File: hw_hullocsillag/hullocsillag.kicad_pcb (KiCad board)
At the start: 2 copper layers, 110 x 56 mm, 38 parts, among them J1 Conn_2Rows-05Pins, Q1 AO3401A, Q2 AO3401A, Q3 AO3401A, SW2 SW_DPST_x2, T1 Tab, T2 Tab, T3 Tab, U1 PY32F002AF15P6TU

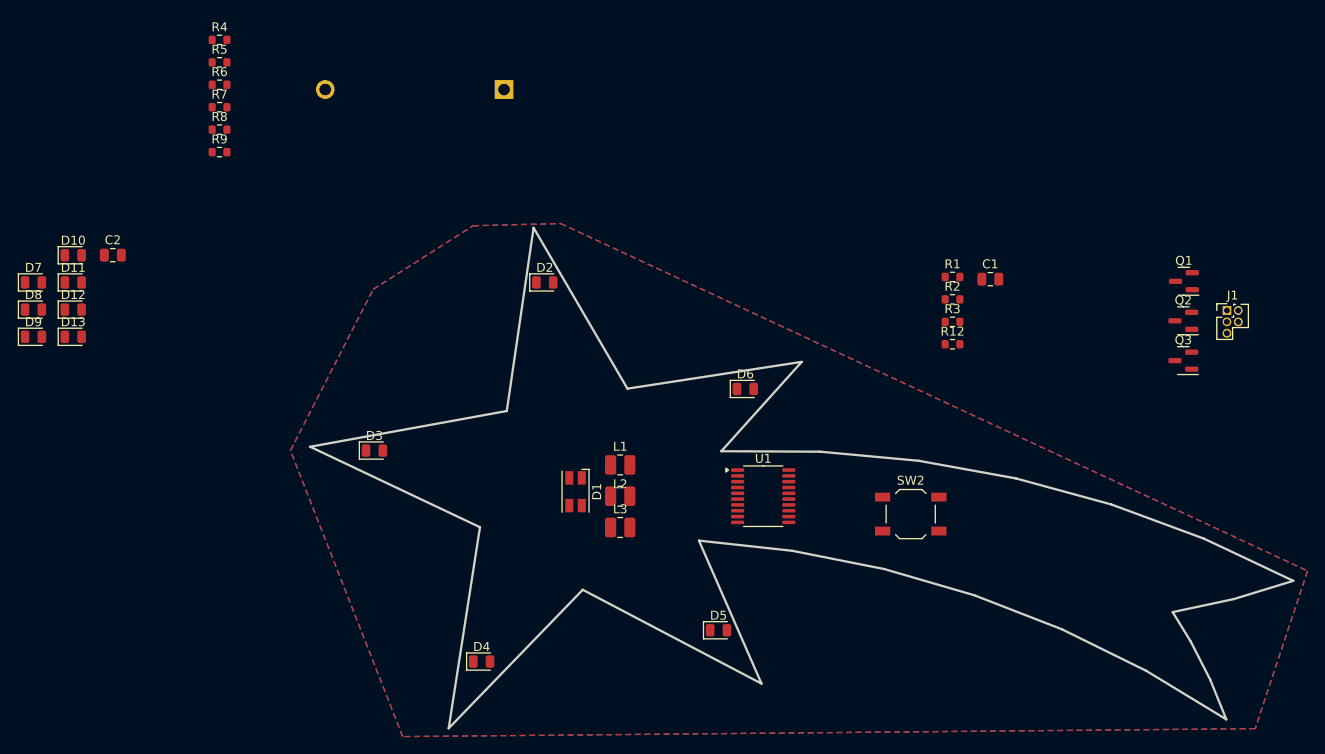
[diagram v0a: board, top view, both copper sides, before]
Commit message: Hullocsillag updated, new led driver
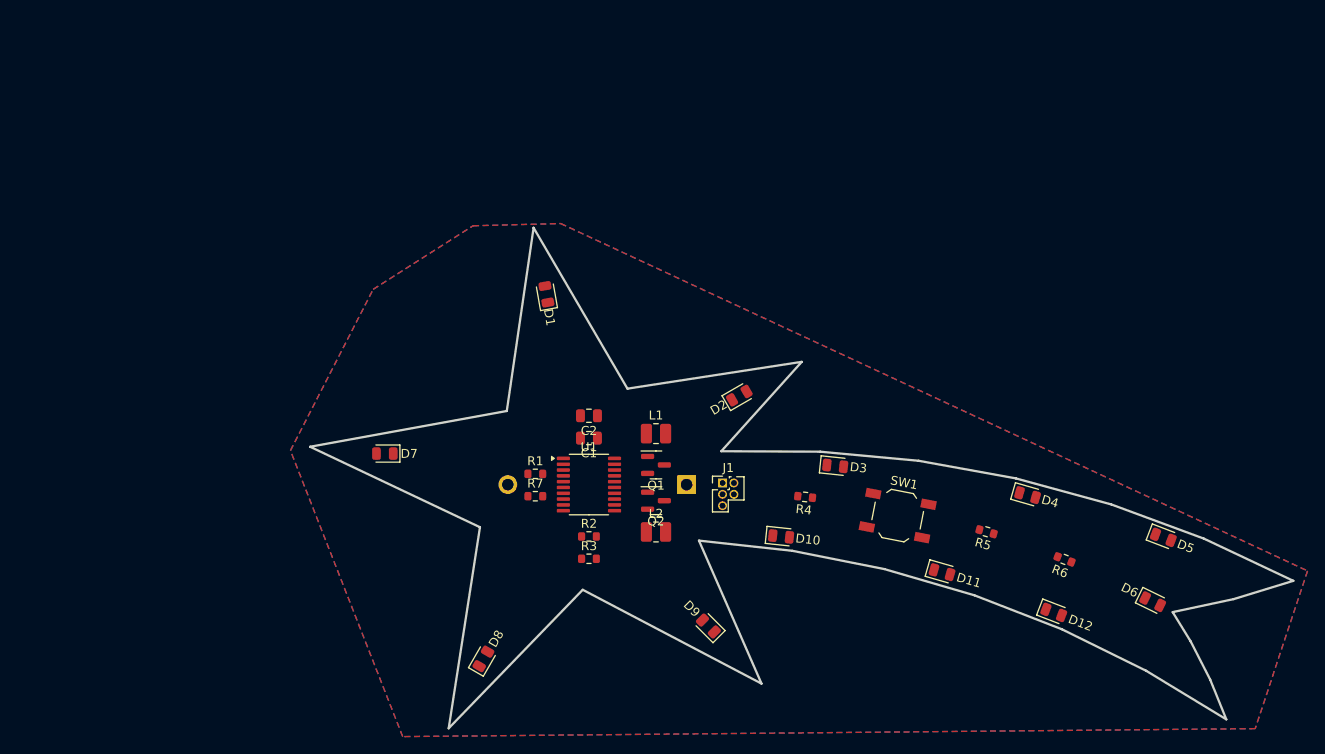
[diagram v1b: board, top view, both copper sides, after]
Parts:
- removed the D1 at (110.0, 93.0)
- removed L3: L, Inductor_SMD:L_1008_2520Metric
- removed Q3: AO3401A, hullocsillag:SOT-23
- removed the R1 at (152.2, 69.0)
- removed R12: 100k, Resistor_SMD:R_0603_1608Metric
- removed the R2 at (152.2, 71.5)
- removed the R3 at (152.2, 74.0)
- added R7: 100k, Resistor_SMD:R_0603_1608Metric, F.Cu at (105.5, 93.5)
- L1, L2: value L -> 1mH
- moved D5 126.0 mm to (175.8, 98.1), turned to -21 degrees
- moved D6 125.1 mm to (174.6, 105.3), turned to -26 degrees
- moved D12 113.9 mm to (163.5, 106.5), turned to -21 degrees
- moved D4 113.1 mm to (160.6, 93.4), turned to -16 degrees
- moved R6 104.9 mm to (164.7, 100.6), turned to 159 degrees
- moved D11 102.5 mm to (151.0, 102.0), turned to -16 degrees
- moved R5 96.9 mm to (156.0, 97.5), turned to 164 degrees
- moved D10 86.6 mm to (133.0, 98.0), turned to -6 degrees
- moved D9 84.7 mm to (124.9, 108.0), turned to 135 degrees
- moved R4 78.7 mm to (135.7, 93.6), turned to 174 degrees
- moved R2 67.2 mm to (111.5, 98.0)
- moved R3 67.2 mm to (111.5, 100.5)
- moved Q1 62.5 mm to (119.0, 90.0), turned to 180 degrees
- moved Q2 62.3 mm to (119.0, 94.0), turned to 180 degrees
- moved R1 60.0 mm to (105.5, 91.0)
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- renumbered D2 to D1, D9 to D10, D13 to D12, D4 to D2, D6 to D3, D8 to D4, D10 to D5, D12 to D6, D3 to D7, D5 to D8, D7 to D9, R4 to R1, R5 to R2, R6 to R3, R7 to R4, R8 to R5, R9 to R6, SW2 to SW1
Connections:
- D1 pad 1: /MPX2 -> Net-(D1-K)
- D10 pad 1: /MPX1 -> Net-(D10-K)
- D11 pad 1: /MPX1 -> Net-(D10-K)
- D12 pad 1: /MPX1 -> Net-(D10-K)
- D2 pad 1: /MPX2 -> Net-(D1-K)
- D3 pad 1: /MPX2 -> Net-(D1-K)
- D4 pad 1: /MPX2 -> Net-(D1-K)
- D5 pad 1: /MPX2 -> Net-(D1-K)
- D6 pad 1: /MPX2 -> Net-(D1-K)
- D7 pad 1: /MPX1 -> Net-(D10-K)
- D8 pad 1: /MPX1 -> Net-(D10-K)
- D9 pad 1: /MPX1 -> Net-(D10-K)
- L1 pad 1: Net-(D1-BK) -> Net-(D1-K)
- L1 pad 2: GND -> /MPX1
- L2 pad 1: Net-(D1-RK) -> Net-(D10-K)
- L2 pad 2: GND -> /MPX2
- Q1 pad 1: /B -> /MPX1
- Q1 pad 3: Net-(D1-BK) -> Net-(D1-K)
- Q2 pad 1: /R -> /MPX2
- Q2 pad 3: Net-(D1-RK) -> Net-(D10-K)
- U1 pad 11: /R -> /MPX1
- U1 pad 12: /B -> /MPX2
- U1 pad 14: /G -> unconnected-(U1-PA3-Pad14)
- U1 pad 6: /MPX1 -> unconnected-(U1-PA6-Pad6)
- U1 pad 7: /MPX2 -> unconnected-(U1-PA5-Pad7)

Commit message: Hullocsillag routed, C2 capacitor relocated, silkscreen added.
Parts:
- moved C2 15.2 mm to (124.7, 92.1), turned to -90 degrees
- moved J1 3.52 mm to (129.1, 94.3), turned to 180 degrees
- moved R1 3.00 mm to (105.5, 90.5)
- moved R2 3.00 mm to (105.5, 94.0)
- turned D7 to 0 degrees
- turned D9 to -45 degrees
- turned L1 to 180 degrees
- turned Q2 to 0 degrees
- turned R4 to 180 degrees
- renumbered R7 to R1, R1 to R2, R2 to R3, R3 to R4, R4 to R5, R5 to R6, R6 to R7
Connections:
- U1 pad 11: /MPX1 -> /MPX2
- U1 pad 12: /MPX2 -> /MPX1
- U1 pad 13: /L1 -> /L2
- U1 pad 15: /L2 -> /L3
- U1 pad 16: /L3 -> /L1
- U1 pad 17: /L4 -> /L6
- U1 pad 19: /L6 -> /L4
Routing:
- net Net-(D10-K): track 0.00 -> 127.8 mm, vias 0 -> 2
- net Net-(D1-K): track 0.00 -> 100.8 mm, vias 0 -> 2
- net GND: track 0.00 -> 77.8 mm, vias 0 -> 17
- net Net-(D3-A): track 0.00 -> 59.6 mm, vias 0 -> 4
- net /L6: track 0.00 -> 56.0 mm, vias 0 -> 2
- net Net-(SW1A-A): track 0.00 -> 54.1 mm, vias 0 -> 2
- net Net-(D2-A): track 0.00 -> 50.9 mm, vias 0 -> 2
- net /L5: track 0.00 -> 46.5 mm, vias 0 -> 2
- net Net-(D1-A): track 0.00 -> 43.4 mm
- net Net-(D10-A): track 0.00 -> 34.0 mm, vias 0 -> 2
- net VCC: track 0.00 -> 32.1 mm, vias 0 -> 2
- net /nRST: track 0.00 -> 31.1 mm, vias 0 -> 1
- net Net-(D11-A): track 0.00 -> 29.1 mm, vias 0 -> 2
- net /SWC: track 0.00 -> 28.6 mm, vias 0 -> 1
- net /SWD: track 0.00 -> 26.0 mm, vias 0 -> 1
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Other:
- board text added: "Every machine is a smoke machine if you operate it wrong enough."
- board text added: "PCB by KaneBear"
- board text added: "Rev.B"
- board text added: "Vesztettem."

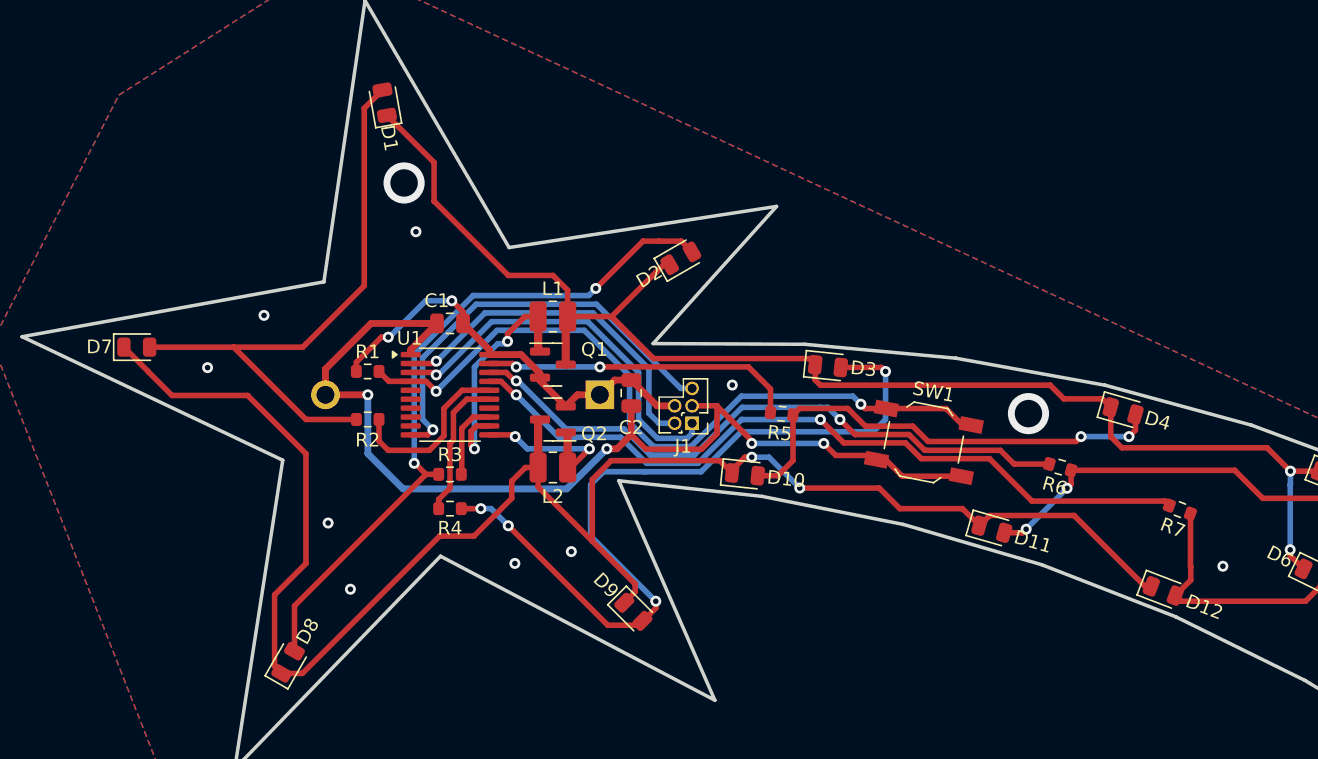
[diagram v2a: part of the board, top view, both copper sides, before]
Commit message: Inductor updated, pull-up resistor added, filling reworked
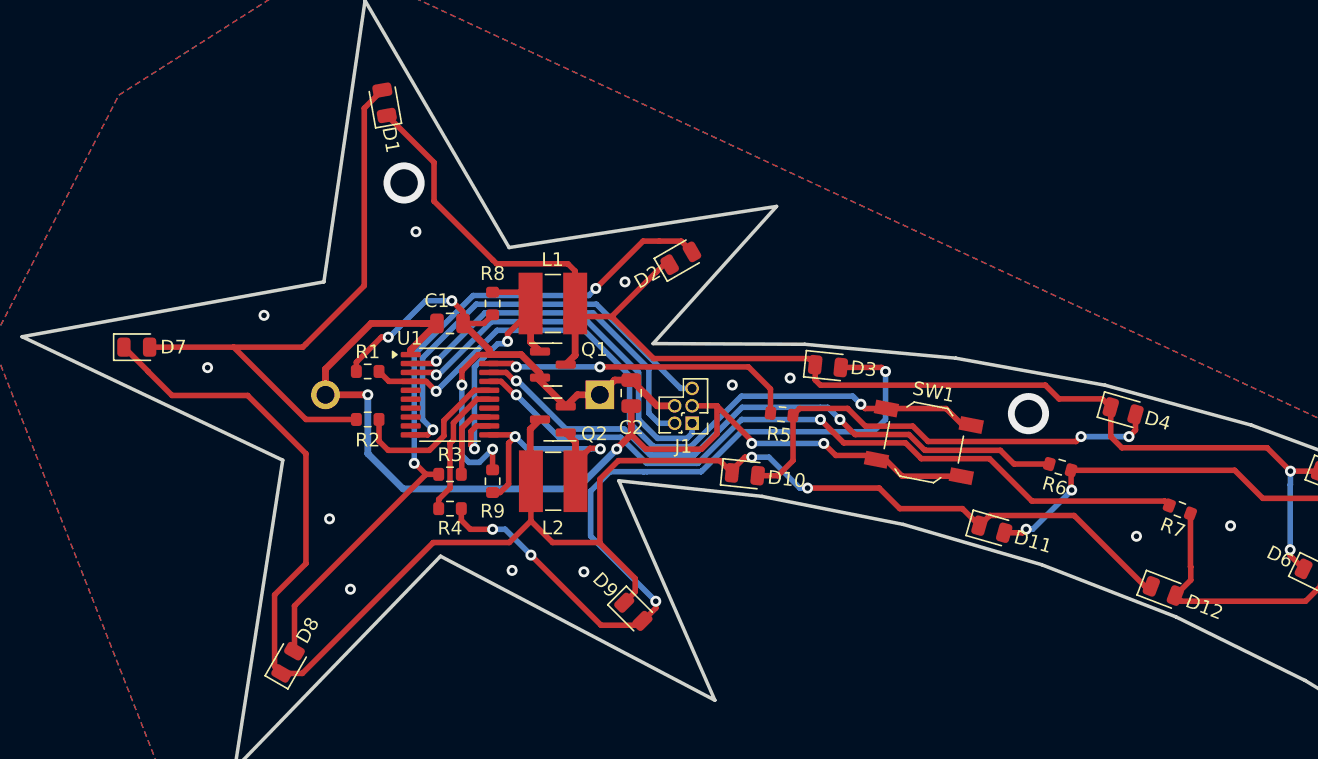
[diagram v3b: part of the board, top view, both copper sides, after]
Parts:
- added R8: 100k, Resistor_SMD:R_0603_1608Metric, F.Cu at (114.6, 85.5)
- added R9: 100k, Resistor_SMD:R_0603_1608Metric, F.Cu at (114.6, 98.5)
- L1, L2: footprint Inductor_SMD:L_1008_2520Metric -> Inductor_SMD:L_Ferrocore_DLG-0403
- T1, T2, T3: footprint kikit:Tab -> PCM_kikit:Tab
- moved L2 1.00 mm to (119.0, 98.5)
- moved L1 0.95 mm to (119.0, 85.5)
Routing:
- net VCC: track 32.1 -> 47.6 mm, vias 2 -> 4
- net /MPX2: track 12.8 -> 20.7 mm
- net /MPX1: track 18.1 -> 22.4 mm
- net Net-(D10-K): track 127.8 -> 131.1 mm
- net Net-(D1-K): track 100.8 -> 102.6 mm
- net /L1: track 12.9 -> 12.4 mm
- net GND: vias 17 -> 20
